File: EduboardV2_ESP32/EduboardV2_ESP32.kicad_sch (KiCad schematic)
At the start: 1 part, among them U1 ESP32-WROOM-E

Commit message: work on debug chip
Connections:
- net TMS: now reaches U1.13 (MTMS/GPIO14/ADC2_CH6)
- net TDI: now reaches U1.14 (MTDI/GPIO12/ADC2_CH5)
- net TCK: now reaches U1.16 (MTCK/GPIO13/ADC2_CH4)
- net TDO: now reaches U1.23 (MTDO/GPIO15/ADC2_CH3)
- net nTRST: now reaches U1.3 (EN/CHIP_PU)
- net TXD: now reaches U1.34 (U0RXD/GPIO3)
- net RXD: now reaches U1.35 (U0TXD/GPIO1)
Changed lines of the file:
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@@
 (kicad_sch (version 20230121) (generator eeschema)
   (paper "A4")
+  (wire (pts (xy 74.295 46.99) (xy 78.105 46.99))
+    (stroke (width 0) (type default))
+  )
+  (wire (pts (xy 73.66 85.09) (xy 78.105 85.09))
+    (stroke (width 0) (type default))
+  )
+  (wire (pts (xy 73.66 82.55) (xy 78.105 82.55))
+    (stroke (width 0) (type default))
+  )
+  (wire (pts (xy 73.66 87.63) (xy 78.105 87.63))
+    (stroke (width 0) (type default))
+  )
+  (wire (pts (xy 74.295 39.37) (xy 78.105 39.37))
+    (stroke (width 0) (type default))
+  )
+  (wire (pts (xy 73.66 80.01) (xy 78.105 80.01))
+    (stroke (width 0) (type default))
+  )
+  (wire (pts (xy 74.295 49.53) (xy 78.105 49.53))
+    (stroke (width 0) (type default))
+  )
+  (global_label "RXD" (shape input) (at 74.295 49.53 180) (fields_autoplaced)
+    (effects (font (size 1.27 1.27)) (justify right))
+    (property "Intersheetrefs" "${INTERSHEET_REFS}" (at 67.6397 49.53 0)
+      (effects (font (size 1.27 1.27)) (justify right) hide)
+    )
+  )
+  (global_label "TCK" (shape output) (at 73.66 85.09 180) (fields_autoplaced)
+    (effects (font (size 1.27 1.27)) (justify right))
+    (property "Intersheetrefs" "${INTERSHEET_REFS}" (at 67.2466 85.09 0)
+      (effects (font (size 1.27 1.27)) (justify right) hide)
+    )
+  )
+  (global_label "TDI" (shape input) (at 73.66 82.55 180) (fields_autoplaced)
+    (effects (font (size 1.27 1.27)) (justify right))
+    (property "Intersheetrefs" "${INTERSHEET_REFS}" (at 67.9118 82.55 0)
+      (effects (font (size 1.27 1.27)) (justify right) hide)
+    )
+  )
+  (global_label "TMS" (shape output) (at 73.66 80.01 180) (fields_autoplaced)
+    (effects (font (size 1.27 1.27)) (justify right))
+    (property "Intersheetrefs" "${INTERSHEET_REFS}" (at 67.1257 80.01 0)
+      (effects (font (size 1.27 1.27)) (justify right) hide)
+    )
+  )
+  (global_label "TDO" (shape output) (at 73.66 87.63 180) (fields_autoplaced)
+    (effects (font (size 1.27 1.27)) (justify right))
+    (property "Intersheetrefs" "${INTERSHEET_REFS}" (at 67.1861 87.63 0)
+      (effects (font (size 1.27 1.27)) (justify right) hide)
+    )
+  )
+  (global_label "TXD" (shape output) (at 74.295 46.99 180) (fields_autoplaced)
+    (effects (font (size 1.27 1.27)) (justify right))
+    (property "Intersheetrefs" "${INTERSHEET_REFS}" (at 67.9421 46.99 0)
+      (effects (font (size 1.27 1.27)) (justify right) hide)
+    )
+  )
+  (global_label "nTRST" (shape output) (at 74.295 39.37 180) (fields_autoplaced)
+    (effects (font (size 1.27 1.27)) (justify right))
+    (property "Intersheetrefs" "${INTERSHEET_REFS}" (at 65.8255 39.37 0)
+      (effects (font (size 1.27 1.27)) (justify right) hide)
+    )
+  )
   (symbol (lib_id "Espressif:ESP32-WROOM-E") (at 111.125 69.85 0) (unit 1)
     (in_bom yes) (on_board yes) (dnp no) (fields_autoplaced)

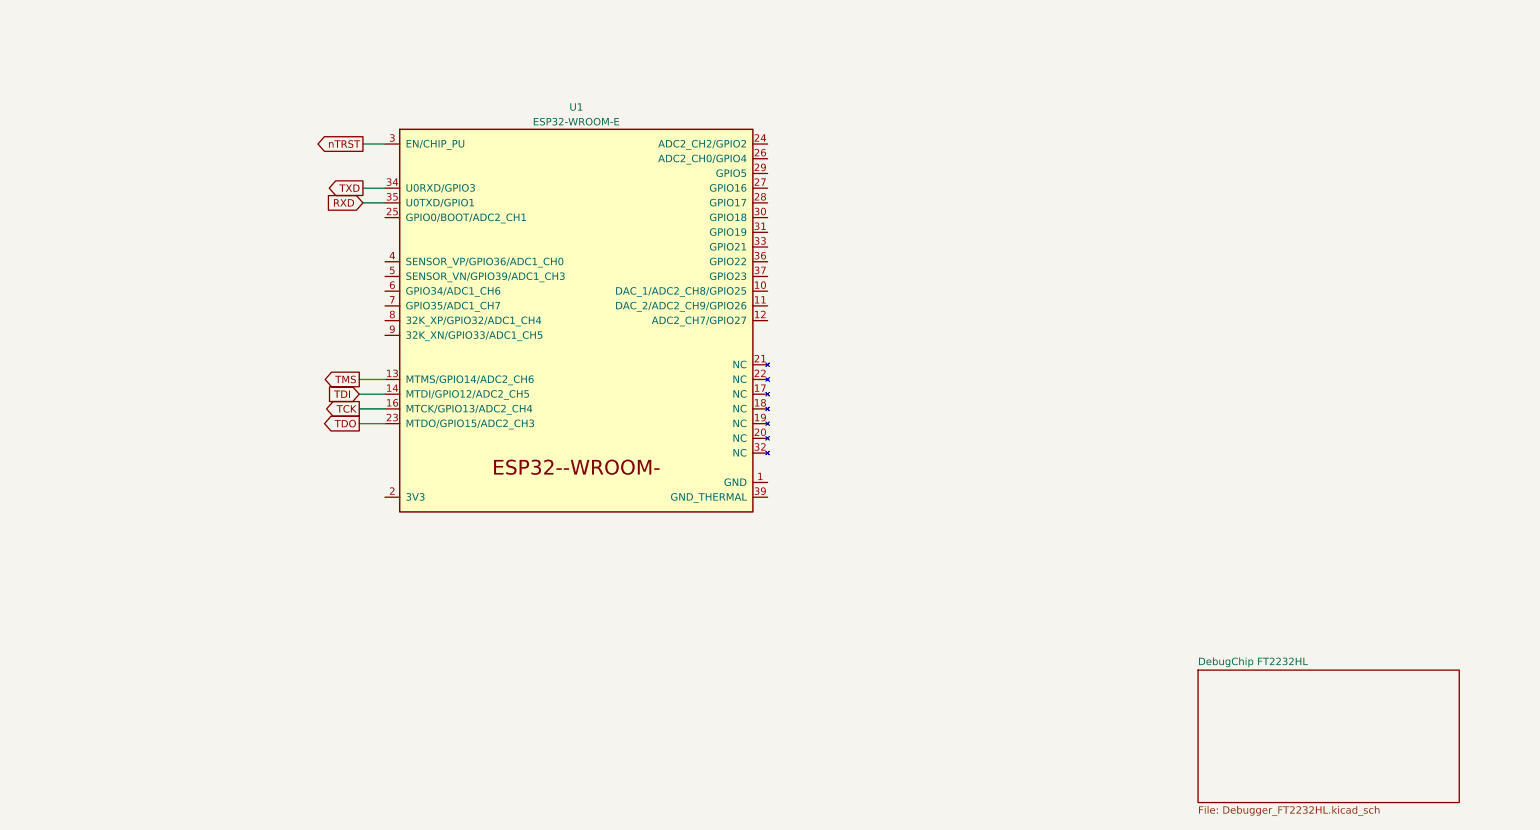
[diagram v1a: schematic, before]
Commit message: finalize ft2232 design, prepare esp pins, work on mpcie pinout
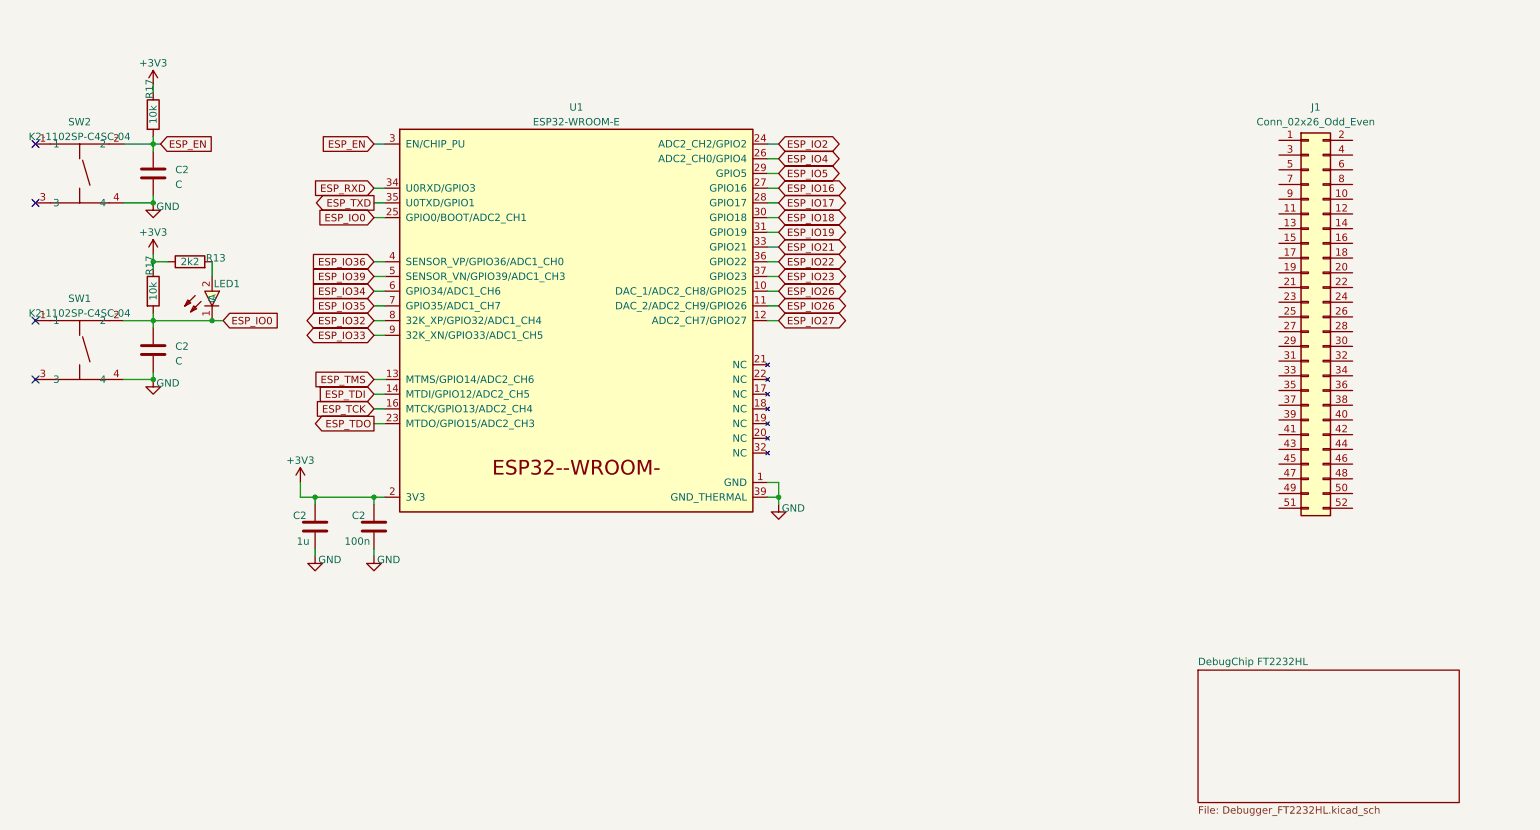
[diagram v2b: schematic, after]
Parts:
- added C2 (x2): C, symbol Device:C
- added C2: 1u, symbol Device:C
- added C2: 100n, symbol Device:C
- added J1: Conn_02x26_Odd_Even, mpcie:mini-PCIe_F1_Full, symbol Connector_Generic:Conn_02x26_Odd_Even
- added LED1: 19-217/BHC-ZL1M2RY/3T, JLCPCB:LED0603-RD, symbol JLCPCB:19-217_BHC-ZL1M2RY_3T
- added R13: 2k2, symbol Device:R
- added R17 (x2): 10k, symbol Device:R
- added SW1, SW2: K2-1102SP-C4SC-04, JLCPCB:KEY-SMD_4P-L6.0-W6.0-P4.50-LS9.5-BL, symbol JLCPCB:K2-1102SP-C4SC-04
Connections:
- net GND: now reaches U1.1 (GND), U1.15 (GND), U1.38 (GND)
- net GND: now also U1.39 (GND_THERMAL), C2.2, C2.2, C2.2, C2.2, SW1.4, SW2.4
- net ESP_IO26: now reaches U1.10 (DAC_1/ADC2_CH8/GPIO25)
- net ESP_IO26: now also U1.11 (DAC_2/ADC2_CH9/GPIO26)
- net ESP_IO27: now reaches U1.12 (ADC2_CH7/GPIO27)
- net +3V3: now reaches U1.2 (3V3)
- net +3V3: now also C2.1, C2.1, R13.1, R17.1, R17.1
- net ESP_IO2: now reaches U1.24 (ADC2_CH2/GPIO2)
- net ESP_IO0: now reaches U1.25 (GPIO0/BOOT/ADC2_CH1)
- net ESP_IO0: now also C2.1, LED1.1 (C), R17.2, SW1.2
- net ESP_IO4: now reaches U1.26 (ADC2_CH0/GPIO4)
- net ESP_IO16: now reaches U1.27 (GPIO16)
- net ESP_IO17: now reaches U1.28 (GPIO17)
- net ESP_IO5: now reaches U1.29 (GPIO5)
- net ESP_IO18: now reaches U1.30 (GPIO18)
- net ESP_IO19: now reaches U1.31 (GPIO19)
- net ESP_IO21: now reaches U1.33 (GPIO21)
- net ESP_IO22: now reaches U1.36 (GPIO22)
- net ESP_IO23: now reaches U1.37 (GPIO23)
- net ESP_IO36: now reaches U1.4 (SENSOR_VP/GPIO36/ADC1_CH0)
- net ESP_IO39: now reaches U1.5 (SENSOR_VN/GPIO39/ADC1_CH3)
- net ESP_IO34: now reaches U1.6 (GPIO34/ADC1_CH6)
- net ESP_IO35: now reaches U1.7 (GPIO35/ADC1_CH7)
- net ESP_IO32: now reaches U1.8 (32K_XP/GPIO32/ADC1_CH4)
- net ESP_IO33: now reaches U1.9 (32K_XN/GPIO33/ADC1_CH5)
- net RXD renamed ESP_TXD
- net TCK renamed ESP_TCK
- net TDI renamed ESP_TDI
- net TDO renamed ESP_TDO
- net TMS renamed ESP_TMS
- net TXD renamed ESP_RXD
- net nTRST renamed ESP_EN
- net ESP_EN: now also C2.1, R17.2, SW2.2
- new net: LED1.2 (A), R13.2
- no-connect marks 0 -> 4

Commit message: add Portexpander, connect mPCIE
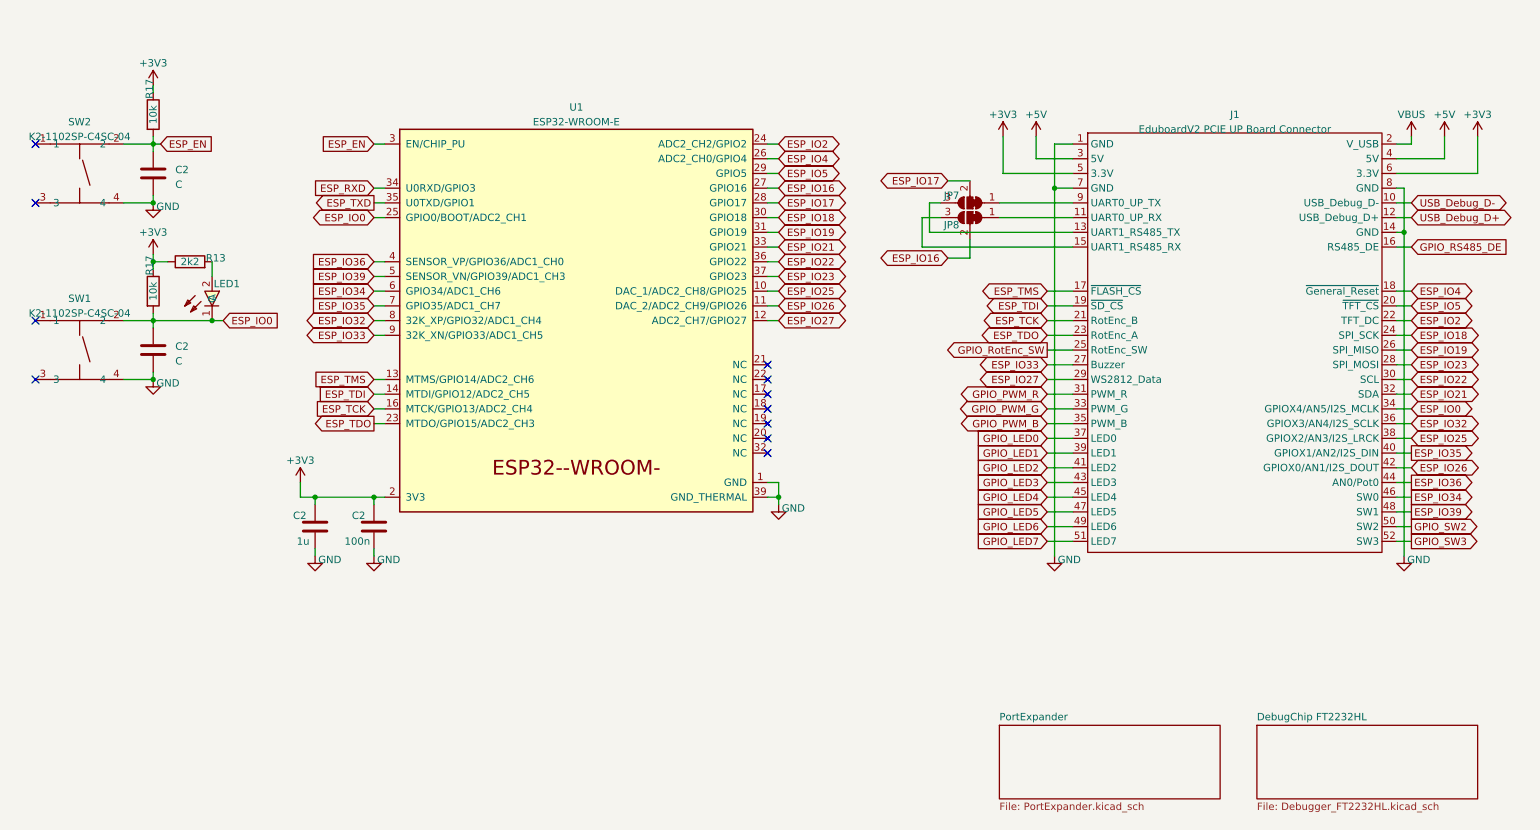
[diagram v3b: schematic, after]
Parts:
- removed J1: Conn_02x26_Odd_Even, mpcie:mini-PCIe_F1_Full, symbol Connector_Generic:Conn_02x26_Odd_Even
- added J1: EduboardV2 PCIE UP Board Connector, EduboardV2_kicadlib:mini-PCIe_F1_Full, symbol EduboardV2_kicadlib:EduboardUPConnector_V1
- added JP7, JP8: SolderJumper_3_Bridged12, symbol Jumper:SolderJumper_3_Bridged12
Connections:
- net +3V3: now also J1.5 (3.3V), J1.6 (3.3V)
- net ESP_IO0: now also J1.34 (GPIOX4/AN5/I2S_MCLK)
- net ESP_IO16: now also JP8.2 (C)
- net ESP_IO17: now also JP7.2 (C)
- net ESP_IO18: now also J1.24 (SPI_SCK)
- net ESP_IO19: now also J1.26 (SPI_MISO)
- net ESP_IO2: now also J1.22 (TFT_DC)
- net ESP_IO21: now also J1.32 (SDA)
- net ESP_IO22: now also J1.30 (SCL)
- net ESP_IO23: now also J1.28 (SPI_MOSI)
- net ESP_IO26: now also J1.42 (GPIOX0/AN1/I2S_DOUT); no longer U1.10 (DAC_1/ADC2_CH8/GPIO25)
- net ESP_IO27: now also J1.29 (WS2812_Data)
- net ESP_IO32: now also J1.36 (GPIOX3/AN4/I2S_SCLK)
- net ESP_IO33: now also J1.27 (Buzzer)
- net ESP_IO34: now also J1.46 (SW0)
- net ESP_IO35: now also J1.40 (GPIOX1/AN2/I2S_DIN)
- net ESP_IO36: now also J1.44 (AN0/Pot0)
- net ESP_IO39: now also J1.48 (SW1)
- net ESP_IO4: now also J1.18 (~{General_Reset})
- net ESP_IO5: now also J1.20 (~{TFT_CS})
- net ESP_TCK: now also J1.21 (RotEnc_B)
- net ESP_TDI: now also J1.19 (~{SD_CS})
- net ESP_TDO: now also J1.23 (RotEnc_A)
- net ESP_TMS: now also J1.17 (~{FLASH_CS})
- net GND: now also J1.1 (GND), J1.14 (GND), J1.7 (GND), J1.8 (GND)
- new net: J1.11 (UART0_UP_RX), JP8.1 (A)
- new net: J1.13 (UART1_RS485_TX), JP7.3 (B)
- new net: J1.15 (UART1_RS485_RX), JP8.3 (B)
- new net: J1.9 (UART0_UP_TX), JP7.1 (A)
- new net +5V: J1.3 (5V), J1.4 (5V)
- new net ESP_IO25: J1.38 (GPIOX2/AN3/I2S_LRCK), U1.10 (DAC_1/ADC2_CH8/GPIO25)
- new net GPIO_LED0: J1.37 (LED0)
- new net GPIO_LED1: J1.39 (LED1)
- new net GPIO_LED2: J1.41 (LED2)
- new net GPIO_LED3: J1.43 (LED3)
- new net GPIO_LED4: J1.45 (LED4)
- new net GPIO_LED5: J1.47 (LED5)
- new net GPIO_LED6: J1.49 (LED6)
- new net GPIO_LED7: J1.51 (LED7)
- new net GPIO_PWM_B: J1.35 (PWM_B)
- new net GPIO_PWM_G: J1.33 (PWM_G)
- new net GPIO_PWM_R: J1.31 (PWM_R)
- new net GPIO_RS485_DE: J1.16 (RS485_DE)
- new net GPIO_RotEnc_SW: J1.25 (RotEnc_SW)
- new net GPIO_SW2: J1.50 (SW2)
- new net GPIO_SW3: J1.52 (SW3)
- new net USB_Debug_D+: J1.12 (USB_Debug_D+)
- new net USB_Debug_D-: J1.10 (USB_Debug_D-)
- new net VBUS: J1.2 (V_USB)
- no-connect marks 4 -> 11
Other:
- added sheet PortExpander (PortExpander.kicad_sch)

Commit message: all parts placed. descision about usb-debug line to be made...
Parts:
- C2: value C -> 100n; footprint (none) -> Capacitor_SMD:C_0603_1608Metric
- C2: footprint (none) -> Capacitor_SMD:C_0603_1608Metric
- JP7, JP8: footprint (none) -> Jumper:SolderJumper-3_P1.3mm_Bridged12_RoundedPad1.0x1.5mm
- LED1: JLCPCB Part # (none) -> C72041
- R13, R17: footprint (none) -> Resistor_SMD:R_0603_1608Metric
- SW1, SW2: JLCPCB Part # (none) -> C127509
- U1: LCSC Part (none) -> C82899
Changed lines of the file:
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@@
       (effects (font (size 1.27 1.27)))
     )
-    (property "Footprint" "" (at 36.322 64.77 90)
+    (property "Footprint" "Resistor_SMD:R_0603_1608Metric" (at 36.322 64.77 90)
       (effects (font (size 1.27 1.27)) hide)
     )
@@
       (effects (font (size 1.27 1.27)) (justify left))
     )
-    (property "Value" "C" (at 41.91 76.835 0)
+    (property "Value" "100n" (at 41.91 76.835 0)
       (effects (font (size 1.27 1.27)) (justify left))
     )
-    (property "Footprint" "" (at 39.0652 78.74 0)
+    (property "Footprint" "Capacitor_SMD:C_0603_1608Metric" (at 39.0652 78.74 0)
       (effects (font (size 1.27 1.27)) hide)
     )
@@
       (effects (font (size 1.27 1.27)))
     )
-    (property "Footprint" "" (at 44.45 61.468 90)
+    (property "Footprint" "Resistor_SMD:R_0603_1608Metric" (at 44.45 61.468 90)
       (effects (font (size 1.27 1.27)) hide)
     )
@@
       (effects (font (size 1.27 1.27)))
     )
-    (property "Footprint" "" (at 36.322 34.29 90)
+    (property "Footprint" "Resistor_SMD:R_0603_1608Metric" (at 36.322 34.29 90)
       (effects (font (size 1.27 1.27)) hide)
     )
@@
       (effects (font (size 1.27 1.27)) hide)
     )
+    (property "JLCPCB Part #" "C72041" (at 46.355 66.04 0)
+      (effects (font (size 1.27 1.27)) hide)
+    )
     (pin "1")
     (pin "2")
@@
     )
     (property "JLC Part" "Extended Part" (at 25.4 97.79 0)
+      (effects (font (size 1.27 1.27)) hide)
+    )
+    (property "JLCPCB Part #" "C127509" (at 25.4 74.93 0)
       (effects (font (size 1.27 1.27)) hide)
     )
@@
       (effects (font (size 1.27 1.27)) (justify left))
     )
-    (property "Footprint" "" (at 67.0052 109.22 0)
+    (property "Footprint" "Capacitor_SMD:C_0603_1608Metric" (at 67.0052 109.22 0)
       (effects (font (size 1.27 1.27)) hide)
     )
@@
       (effects (font (size 1.27 1.27)) (justify left))
     )
-    (property "Footprint" "" (at 77.1652 109.22 0)
+    (property "Footprint" "Capacitor_SMD:C_0603_1608Metric" (at 77.1652 109.22 0)
       (effects (font (size 1.27 1.27)) hide)
     )
@@
       (effects (font (size 1.27 1.27)) hide)
     )
-    (property "Footprint" "" (at 179.07 52.07 0)
+    (property "Footprint" "Jumper:SolderJumper-3_P1.3mm_Bridged12_RoundedPad1.0x1.5mm" (at 179.07 52.07 0)
       (effects (font (size 1.27 1.27)) hide)
     )
@@
       (effects (font (size 1.27 1.27)) hide)
     )
-    (property "Footprint" "" (at 179.07 49.53 0)
+    (property "Footprint" "Jumper:SolderJumper-3_P1.3mm_Bridged12_RoundedPad1.0x1.5mm" (at 179.07 49.53 0)
       (effects (font (size 1.27 1.27)) hide)
     )
@@
     )
     (property "JLC Part" "Extended Part" (at 25.4 67.31 0)
+      (effects (font (size 1.27 1.27)) hide)
+    )
+    (property "JLCPCB Part #" "C127509" (at 25.4 44.45 0)
       (effects (font (size 1.27 1.27)) hide)
     )
@@
     )
     (property "JLCPCB Part #" "C82899" (at 111.125 69.85 0)
+      (effects (font (size 1.27 1.27)) hide)
+    )
+    (property "LCSC Part" "C82899" (at 111.125 69.85 0)
       (effects (font (size 1.27 1.27)) hide)
     )
@@
       (effects (font (size 1.27 1.27)) (justify left))
     )
-    (property "Value" "C" (at 41.91 46.355 0)
+    (property "Value" "100n" (at 41.91 46.355 0)
       (effects (font (size 1.27 1.27)) (justify left))
     )
-    (property "Footprint" "" (at 39.0652 48.26 0)
-      (effects (font (size 1.27 1.27)) hide)
-    )
+    (property "Footprint" "Capacitor_SMD:C_0603_1608Metric" (at 39.0652 48.26 0)
+      (effects (font (size 1.27 1.27)) hide)
+    )

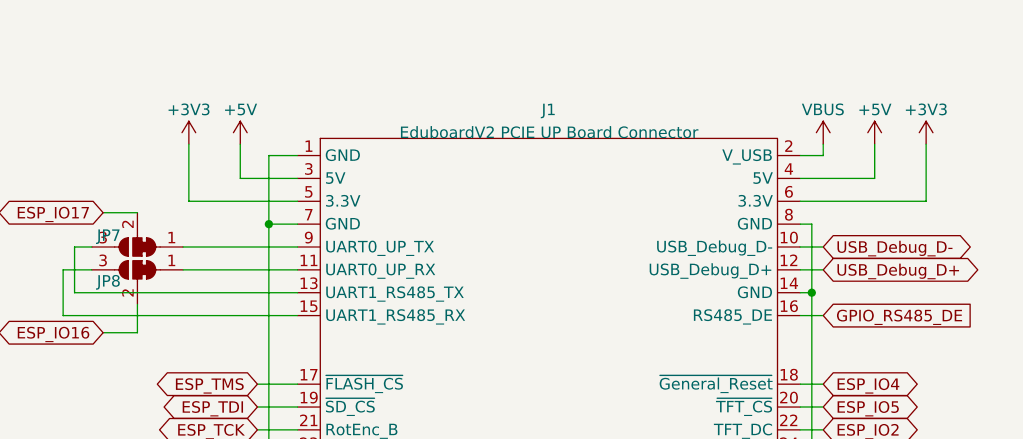
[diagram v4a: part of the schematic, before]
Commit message: add voltage selector to prevent fighting sources
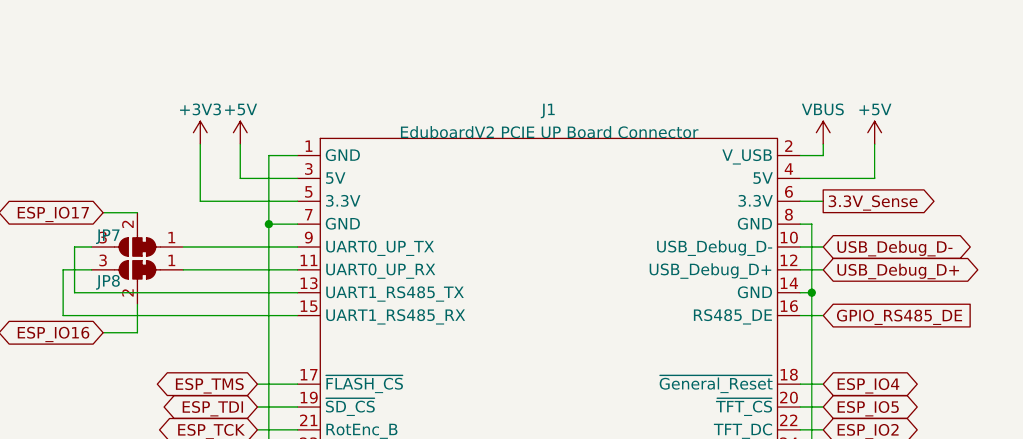
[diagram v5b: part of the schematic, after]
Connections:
- net +3V3: no longer J1.6 (3.3V)
- new net 3.3V_Sense: J1.6 (3.3V)
